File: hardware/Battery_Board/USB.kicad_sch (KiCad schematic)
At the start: 27 parts, among them J3 Battery, P1 USB_C_Plug_USB2.0, Q1 DMG3415U-7, SW3 ON, U4 TP4056

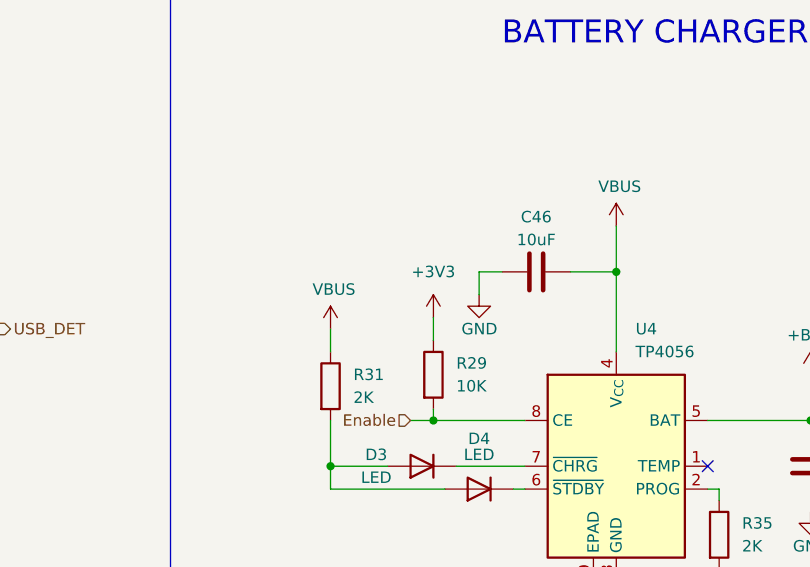
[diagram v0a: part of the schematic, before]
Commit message: feat(Hw):Update_Battery_Sch_And_Sensors_And_PWNCube
pending_Outputs_connectors
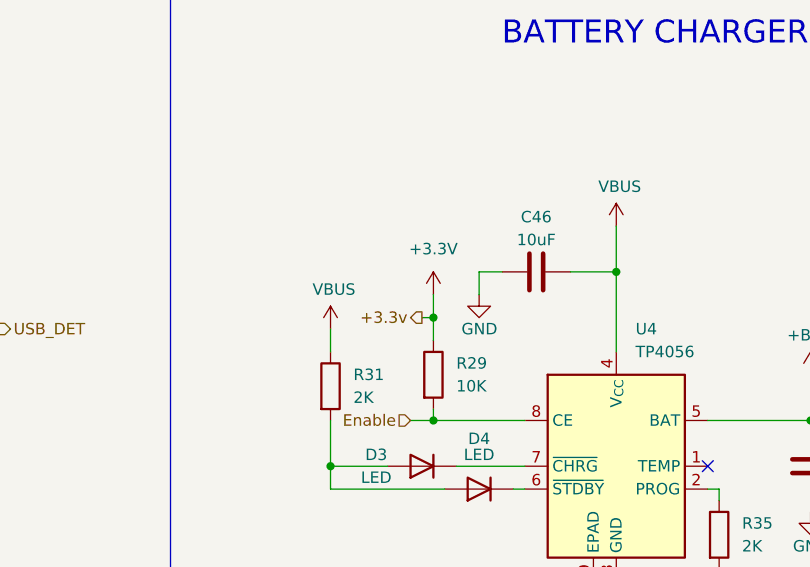
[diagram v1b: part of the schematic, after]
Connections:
- net +3V3 renamed +3.3V
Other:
- company: (none) -> Electronic Cats
- title: (none) -> Battery_Board
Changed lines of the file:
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@@
 	(generator_version "9.0")
 	(paper "A4")
+	(title_block
+		(title "Battery_Board")
+		(date "2026-01-23")
+		(rev "1.0")
+		(company "Electronic Cats")
+		(comment 1 "Edgar Capuchino")
+	)
 	(text "USB-C\n"
 		(exclude_from_sim no)
@@
 	)
 	(junction
+		(at 146.05 50.8)
+		(diameter 0)
+		(color 0 0 0 0)
+	)
+	(junction
 		(at 187.96 62.23)
 		(diameter 0)
@@
 	(wire
 		(pts
-			(xy 146.05 50.8) (xy 146.05 53.34)
+			(xy 146.05 48.26) (xy 146.05 50.8)
 		)
 		(stroke
@@
 	(wire
 		(pts
+			(xy 144.78 50.8) (xy 146.05 50.8)
+		)
+		(stroke
+			(width 0)
+			(type default)
+		)
+	)
+	(wire
+		(pts
 			(xy 48.26 41.91) (xy 50.8 41.91)
 		)
@@
 	(wire
 		(pts
+			(xy 146.05 50.8) (xy 146.05 53.34)
+		)
+		(stroke
+			(width 0)
+			(type default)
+		)
+	)
+	(wire
+		(pts
 			(xy 207.01 52.07) (xy 207.01 54.61)
 		)
@@
 		)
 	)
+	(hierarchical_label "+3.3v"
+		(shape output)
+		(at 144.78 50.8 180)
+		(effects
+			(font
+				(size 1.27 1.27)
+			)
+			(justify right)
+		)
+	)
 	(symbol
 		(lib_id "power:VBUS")
@@
 	)
 	(symbol
-		(lib_id "power:+3V3")
-		(at 146.05 50.8 0)
-		(unit 1)
-		(exclude_from_sim no)
-		(in_bom yes)
-		(on_board yes)
-		(dnp no)
-		(fields_autoplaced yes)
-		(property "Reference" "#PWR075"
-			(at 146.05 54.61 0)
-			(effects
-				(font
-					(size 1.27 1.27)
-				)
-				(hide yes)
-			)
-		)
-		(property "Value" "+3V3"
-			(at 146.05 45.72 0)
-			(effects
-				(font
-					(size 1.27 1.27)
-				)
-			)
-		)
-		(property "Footprint" ""
-			(at 146.05 50.8 0)
-			(effects
-				(font
-					(size 1.27 1.27)
-				)
-				(hide yes)
-			)
-		)
-		(property "Datasheet" ""
-			(at 146.05 50.8 0)
-			(effects
-				(font
-					(size 1.27 1.27)
-				)
-				(hide yes)
-			)
-		)
-		(property "Description" "Power symbol creates a global label with name \"+3V3\""
-			(at 146.05 50.8 0)
-			(effects
-				(font
-					(size 1.27 1.27)
-				)
-				(hide yes)
-			)
-		)
-		(pin "1"
-		)
-		(instances
-			(project "Battery_Board"
-				(path "/575e3b02-8b1c-4d49-bab4-a07d6288bebf/1451f59f-2b56-4011-b9cc-b834ac47899f"
-					(reference "#PWR075")
-					(unit 1)
-				)
-			)
-		)
-	)
-	(symbol
 		(lib_id "Device:R")
 		(at 207.01 58.42 0)
@@
 					(unit 1)
 				)
+			)
+		)
+	)
+	(symbol
+		(lib_id "power:+3.3V")
+		(at 146.05 48.26 0)
+		(unit 1)
+		(exclude_from_sim no)
+		(in_bom yes)
+		(on_board yes)
+		(dnp no)
+		(fields_autoplaced yes)
+		(property "Reference" "#PWR0105"
+			(at 146.05 52.07 0)
+			(effects
+				(font
+					(size 1.27 1.27)
+				)
+				(hide yes)
+			)
+		)
+		(property "Value" "+3.3V"
+			(at 146.05 43.18 0)
+			(effects
+				(font
+					(size 1.27 1.27)
+				)
+			)
+		)
+		(property "Footprint" ""
+			(at 146.05 48.26 0)
+			(effects
+				(font
+					(size 1.27 1.27)
+				)
+				(hide yes)
+			)
+		)
+		(property "Datasheet" ""
+			(at 146.05 48.26 0)
+			(effects
+				(font
+					(size 1.27 1.27)
+				)
+				(hide yes)
+			)
+		)
+		(property "Description" "Power symbol creates a global label with name \"+3.3V\""
+			(at 146.05 48.26 0)
+			(effects
+				(font
+					(size 1.27 1.27)
+				)
+				(hide yes)
+			)
+		)
+		(pin "1"
+		)
+		(instances
+			(project "Battery_Board"
+				(path "/575e3b02-8b1c-4d49-bab4-a07d6288bebf/1451f59f-2b56-4011-b9cc-b834ac47899f"
+					(reference "#PWR0105")
+					(unit 1)
+				)

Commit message: feat(Hw):BoM´s_Updated
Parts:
- R28: now in the parts list
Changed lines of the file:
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@@
 		(unit 1)
 		(exclude_from_sim no)
-		(in_bom no)
+		(in_bom yes)
 		(on_board yes)
 		(dnp no)
